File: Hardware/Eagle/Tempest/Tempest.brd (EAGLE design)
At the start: 110 x 16 mm, 62 parts, among them CON1 B3B-ZR, CON2 B2B-ZR, CON3 B4B-ZR, CON4 HDR2MM-8, CON5 HDR2MM-8, CON6 USB-MICRO-A, CON7 FE05-2HD-2, IC1 ATSAMD21E, IC2 MMA8652, IC3 TPS62150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

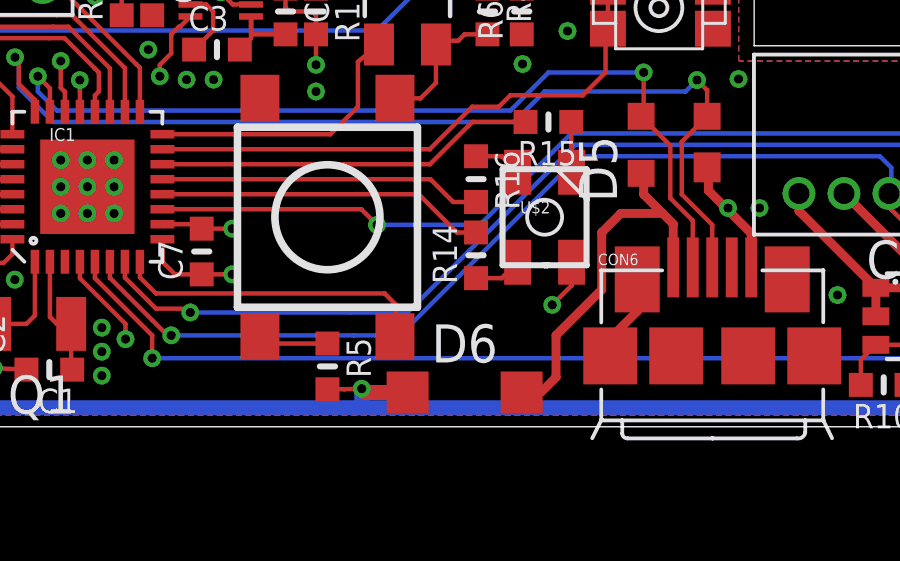
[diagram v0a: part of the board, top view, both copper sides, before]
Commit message: - Added 100K between power button and controller - Added part # for fets and diodes
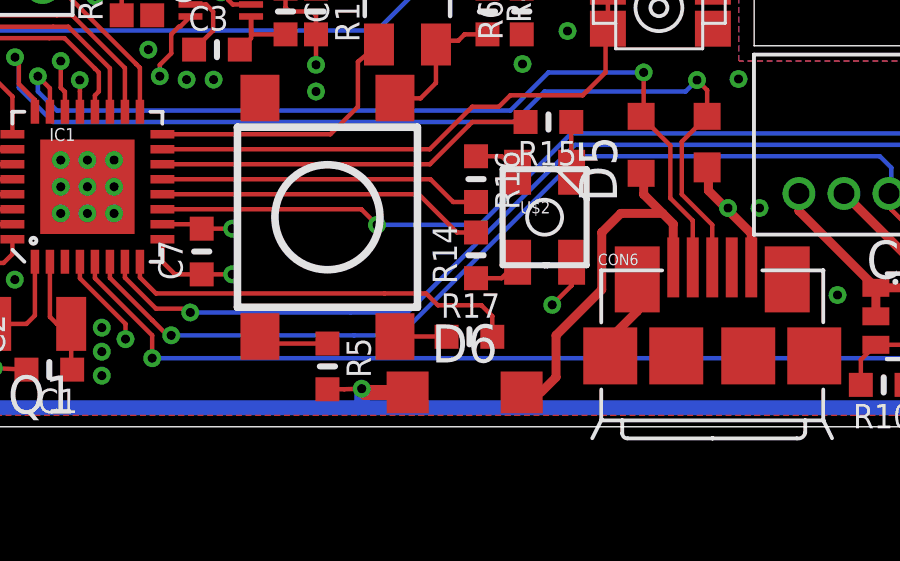
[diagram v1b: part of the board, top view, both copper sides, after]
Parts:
- added R17: 100k, squirrel:_0603MP
- D1, D2, D6: value SOD123 -> PMEG4010ETR
- D4: value (none) -> BZT52C20
- T1, T2: value (none) -> ZXMN3A03E6
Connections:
- new net N$8: R17.1, SW1.A1
- net SAM_SW: now also R17.2; no longer SW1.A1
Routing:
- net SAM_SW: track 10.5 -> 13.5 mm
- net N$8: track 0.00 -> 1.73 mm
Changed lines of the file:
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@@
 </autorouter>
 <elements>
-<element name="T1" library="squirrel" package="SOT23-6" value="" x="100.711" y="4.572" rot="R180"/>
-<element name="T2" library="squirrel" package="SOT23-6" value="" x="91.948" y="3.683" rot="R270"/>
+<element name="T1" library="squirrel" package="SOT23-6" value="ZXMN3A03E6" x="100.711" y="4.572" rot="R180"/>
+<element name="T2" library="squirrel" package="SOT23-6" value="ZXMN3A03E6" x="91.948" y="3.683" rot="R270"/>
 <element name="C14" library="squirrel" package="C1206" value="10µ" x="54.737" y="5.207" rot="R90"/>
 <element name="C15" library="squirrel" package="C1206" value="22µ" x="54.737" y="10.287" rot="R270"/>
@@
 <element name="C1" library="squirrel" package="_0603MP" value="22p" x="63.246" y="1.905" rot="R180"/>
 <element name="C2" library="squirrel" package="_0603MP" value="22p" x="60.325" y="2.794" rot="R270"/>
-<element name="D1" library="squirrel" package="SOD123" value="SOD123" x="55.118" y="1.27" rot="R180"/>
-<element name="D2" library="squirrel" package="SOD123" value="SOD123" x="105.156" y="3.429" rot="R180"/>
-<element name="D4" library="squirrel" package="SOD123" value="" x="105.156" y="1.27" rot="R180"/>
-<element name="D6" library="squirrel" package="SOD123" value="SOD123" x="77.089" y="1.143"/>
+<element name="D1" library="squirrel" package="SOD123" value="PMEG4010ETR" x="55.118" y="1.27" rot="R180"/>
+<element name="D2" library="squirrel" package="SOD123" value="PMEG4010ETR" x="105.156" y="3.429" rot="R180"/>
+<element name="D4" library="squirrel" package="SOD123" value="BZT52C20" x="105.156" y="1.27" rot="R180"/>
+<element name="D6" library="squirrel" package="SOD123" value="PMEG4010ETR" x="77.089" y="1.143"/>
 <element name="CON4" library="squirrel" package="HDR2MM-8" value="HDR2MM-8" x="49.022" y="14.732"/>
 <element name="R6" library="squirrel" package="_0603MP" value="100K" x="78.994" y="13.843" rot="R90"/>
@@
 <element name="FID5" library="squirrel" package="MICRO-FIDUCIAL" value="FIDUCIALUFIDUCIAL" x="42.157" y="0.649" rot="R270"/>
 <element name="FID6" library="squirrel" package="MICRO-FIDUCIAL" value="FIDUCIALUFIDUCIAL" x="45.72" y="0.648" rot="R270"/>
+<element name="R17" library="squirrel" package="_0603MP" value="100k" x="77.25" y="3"/>
 </elements>
 <signals>
@@
 <wire x1="66.266" y1="4.981" x2="66.802" y2="4.445" width="0.15" layer="1"/>
 <wire x1="66.802" y1="4.445" x2="74.422" y2="4.445" width="0.15" layer="1"/>
-<wire x1="74.422" y1="4.445" x2="74.803" y2="4.064" width="0.15" layer="1"/>
-<wire x1="74.803" y1="4.064" x2="74.803" y2="3.046" width="0.15" layer="1"/>
-<contactref element="SW1" pad="A1"/>
-<wire x1="74.803" y1="3.046" x2="74.767" y2="3.01" width="0.15" layer="1"/>
+<contactref element="R17" pad="2"/>
+<wire x1="78.012" y1="3" x2="78.012" y2="3.688" width="0.15" layer="1"/>
+<wire x1="78.012" y1="3.688" x2="77.65" y2="4.05" width="0.15" layer="1"/>
+<wire x1="77.65" y1="4.05" x2="76.2" y2="4.05" width="0.15" layer="1"/>
+<wire x1="74.422" y1="4.445" x2="75.805" y2="4.445" width="0.15" layer="1"/>
+<wire x1="75.805" y1="4.445" x2="76.2" y2="4.05" width="0.15" layer="1"/>
 </signal>
 <signal name="SAM_PWR_EN">
@@
 <wire x1="65.766" y1="10.501" x2="65.766" y2="11.958" width="0.15" layer="1"/>
 </signal>
+<signal name="N$8">
+<contactref element="SW1" pad="A1"/>
+<contactref element="R17" pad="1"/>
+<wire x1="74.767" y1="3.01" x2="76.488" y2="3.01" width="0.15" layer="1"/>
+<wire x1="76.488" y1="3.01" x2="76.488" y2="3" width="0.15" layer="1"/>
+</signal>
 </signals>
